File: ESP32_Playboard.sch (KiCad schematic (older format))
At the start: 40 parts, among them J1 USB_B_Micro, J2 TF_PUSH, Q1 Q_NPN_BEC, Q2 Q_NPN_BEC, Q3 Q_NPN_BEC, SW1 SW_SPST, SW2 SW_SPST, U1 AMS1117-3.3, U2 USBLC6-2SC6, U3 CH340G, U4 ESP32-WROVER-I, U5 MPU-6050, U6 SHT30-DIS, Y1 12MHz

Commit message: Finished PCB layout
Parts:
- added H2, H3: MountingHole, MountingHole:MountingHole_3.2mm_M3, symbol Mechanical:MountingHole
- renumbered C8 to C10, C9 to C11, C10 to C8, C11 to C9, U5 to U4, U4 to U5
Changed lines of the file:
@@
 	9800 3900 9800 4150
 $Comp
-L power:GND #PWR011
+L power:GND #PWR010
 U 1 1 62176701
 P 9200 4100
-F 0 "#PWR011" H 9200 3850 50  0001 C CNN
+F 0 "#PWR010" H 9200 3850 50  0001 C CNN
 F 1 "GND" H 9205 3927 50  0000 C CNN
 F 2 "" H 9200 4100 50  0001 C CNN
@@
 $EndComp
 $Comp
-L Sensor_Motion:MPU-6050 U5
+L Sensor_Motion:MPU-6050 U4
 U 1 1 61F460D4
 P 9900 4850
-F 0 "U5" H 9450 5400 50  0000 C CNN
+F 0 "U4" H 9450 5400 50  0000 C CNN
 F 1 "MPU-6050" H 10300 5400 50  0000 C CNN
 F 2 "Sensor_Motion:InvenSense_QFN-24_4x4mm_P0.5mm" H 9900 4050 50  0001 C CNN
@@
 $EndComp
 $Comp
-L Device:C_Small C10
+L Device:C_Small C8
 U 1 1 620A695E
 P 9200 4000
-F 0 "C10" H 9300 4050 50  0000 C CNN
+F 0 "C8" H 9300 4050 50  0000 C CNN
 F 1 "10nF" H 9350 3950 50  0000 C CNN
 F 2 "Capacitor_SMD:C_0603_1608Metric" H 9200 4000 50  0001 C CNN
@@
 Connection ~ 9800 3900
 $Comp
-L Device:C_Small C11
+L Device:C_Small C9
 U 1 1 622611E6
 P 10700 4000
-F 0 "C11" H 10500 4000 50  0000 L CNN
+F 0 "C9" H 10500 4000 50  0000 L CNN
 F 1 "100nF" H 10450 3900 50  0000 L CNN
 F 2 "Capacitor_SMD:C_0603_1608Metric" H 10700 4000 50  0001 C CNN
@@
 Connection ~ 10000 3900
 $Comp
-L power:GND #PWR012
+L power:GND #PWR011
 U 1 1 62270878
 P 10700 4100
-F 0 "#PWR012" H 10700 3850 50  0001 C CNN
+F 0 "#PWR011" H 10700 3850 50  0001 C CNN
 F 1 "GND" H 10705 3927 50  0000 C CNN
 F 2 "" H 10700 4100 50  0001 C CNN
@@
 $EndComp
 $Comp
-L power:GND #PWR021
+L power:GND #PWR020
 U 1 1 62306E82
 P 9900 5550
-F 0 "#PWR021" H 9900 5300 50  0001 C CNN
+F 0 "#PWR020" H 9900 5300 50  0001 C CNN
 F 1 "GND" H 9905 5377 50  0000 C CNN
 F 2 "" H 9900 5550 50  0001 C CNN
@@
 REG_3V3
 $Comp
-L Device:C_Small C8
+L Device:C_Small C10
 U 1 1 61BF902D
 P 2600 4150
-F 0 "C8" H 2800 4100 50  0000 R CNN
+F 0 "C10" H 2800 4100 50  0000 R CNN
 F 1 "22uF" H 2900 4200 50  0000 R CNN
 F 2 "Capacitor_SMD:C_0603_1608Metric" H 2600 4150 50  0001 C CNN
@@
 $EndComp
 $Comp
-L Device:C_Small C9
+L Device:C_Small C11
 U 1 1 61BF9804
 P 2800 4150
-F 0 "C9" H 2700 4100 50  0000 R CNN
+F 0 "C11" H 2700 4100 50  0000 R CNN
 F 1 "100nF" H 2700 4200 50  0000 R CNN
 F 2 "Capacitor_SMD:C_0603_1608Metric" H 2800 4150 50  0001 C CNN
@@
 	2800 4300 2800 4250
 $Comp
-L power:GND #PWR010
+L power:GND #PWR012
 U 1 1 61C2302B
 P 2700 4350
-F 0 "#PWR010" H 2700 4100 50  0001 C CNN
+F 0 "#PWR012" H 2700 4100 50  0001 C CNN
 F 1 "GND" H 2705 4177 50  0000 C CNN
 F 2 "" H 2700 4350 50  0001 C CNN
@@
 IR_RECV
 $Comp
-L power:GND #PWR020
+L power:GND #PWR021
 U 1 1 61CED5C0
 P 4800 5700
-F 0 "#PWR020" H 4800 5450 50  0001 C CNN
+F 0 "#PWR021" H 4800 5450 50  0001 C CNN
 F 1 "GND" H 4805 5527 50  0000 C CNN
 F 2 "" H 4800 5700 50  0001 C CNN
@@
 ESP_RX
 $Comp
-L PlayboardLib:ESP32-WROVER-I U4
+L PlayboardLib:ESP32-WROVER-I U5
 U 1 1 61BE7406
 P 4150 5100
-F 0 "U4" H 4150 6467 50  0000 C CNN
+F 0 "U5" H 4150 6467 50  0000 C CNN
 F 1 "ESP32-WROVER-I" H 4150 6376 50  0000 C CNN
 F 2 "PlayboardLib:XCVR_ESP32-WROVER-I" H 3850 6350 50  0001 L BNN
@@
 	1    0    0    -1
 $EndComp
+$Comp
+L Mechanical:MountingHole H2
+U 1 1 61F4E6C6
+P 11050 600
+F 0 "H2" H 11150 646 50  0000 L CNN
+F 1 "MountingHole" H 11150 555 50  0000 L CNN
+F 2 "MountingHole:MountingHole_3.2mm_M3" H 11050 600 50  0001 C CNN
+F 3 "~" H 11050 600 50  0001 C CNN
+	1    11050 600
+	1    0    0    -1
+$EndComp
+$Comp
+L Mechanical:MountingHole H3
+U 1 1 61F5140B
+P 10800 600
+F 0 "H3" H 10900 646 50  0000 L CNN
+F 1 "MountingHole" H 10900 555 50  0000 L CNN
+F 2 "MountingHole:MountingHole_3.2mm_M3" H 10800 600 50  0001 C CNN
+F 3 "~" H 10800 600 50  0001 C CNN
+	1    10800 600
+	1    0    0    -1
+$EndComp

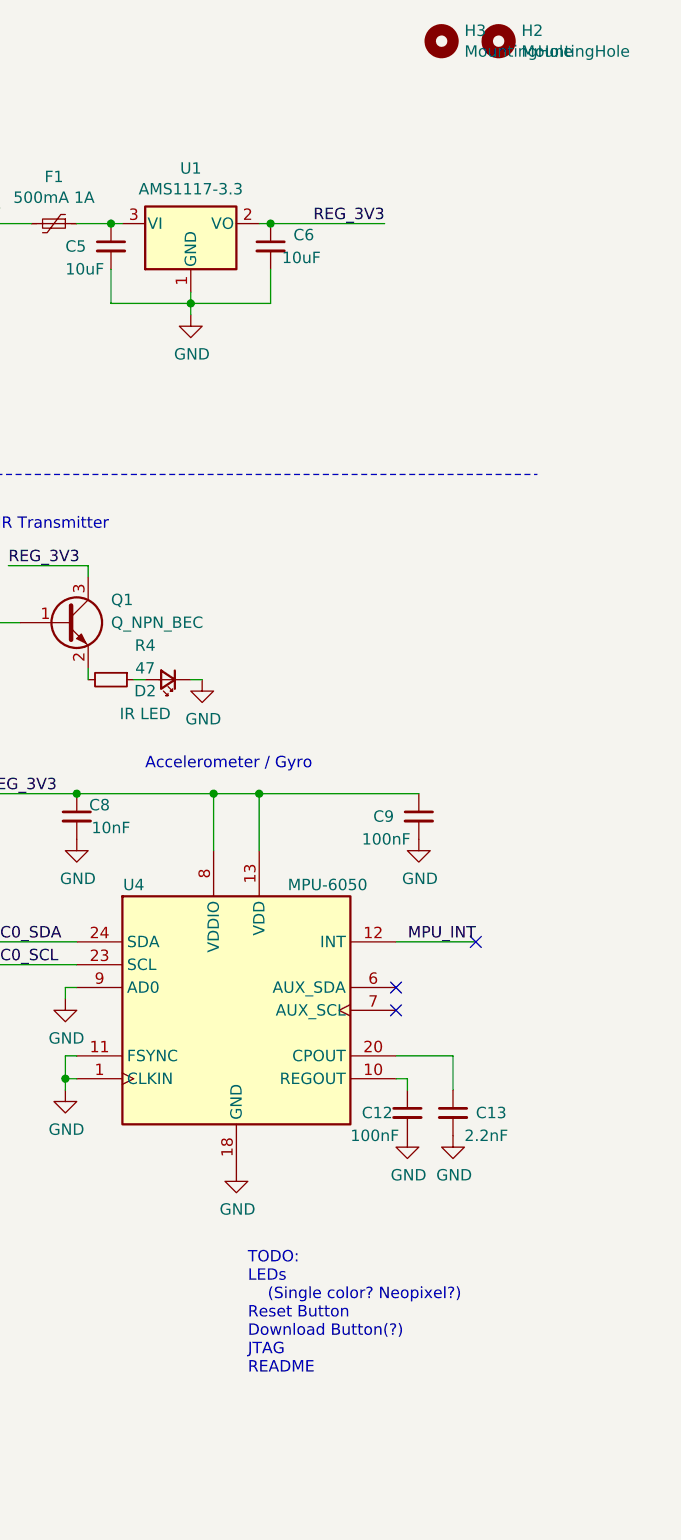
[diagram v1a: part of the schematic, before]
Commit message: Exported Gerber and started Readme
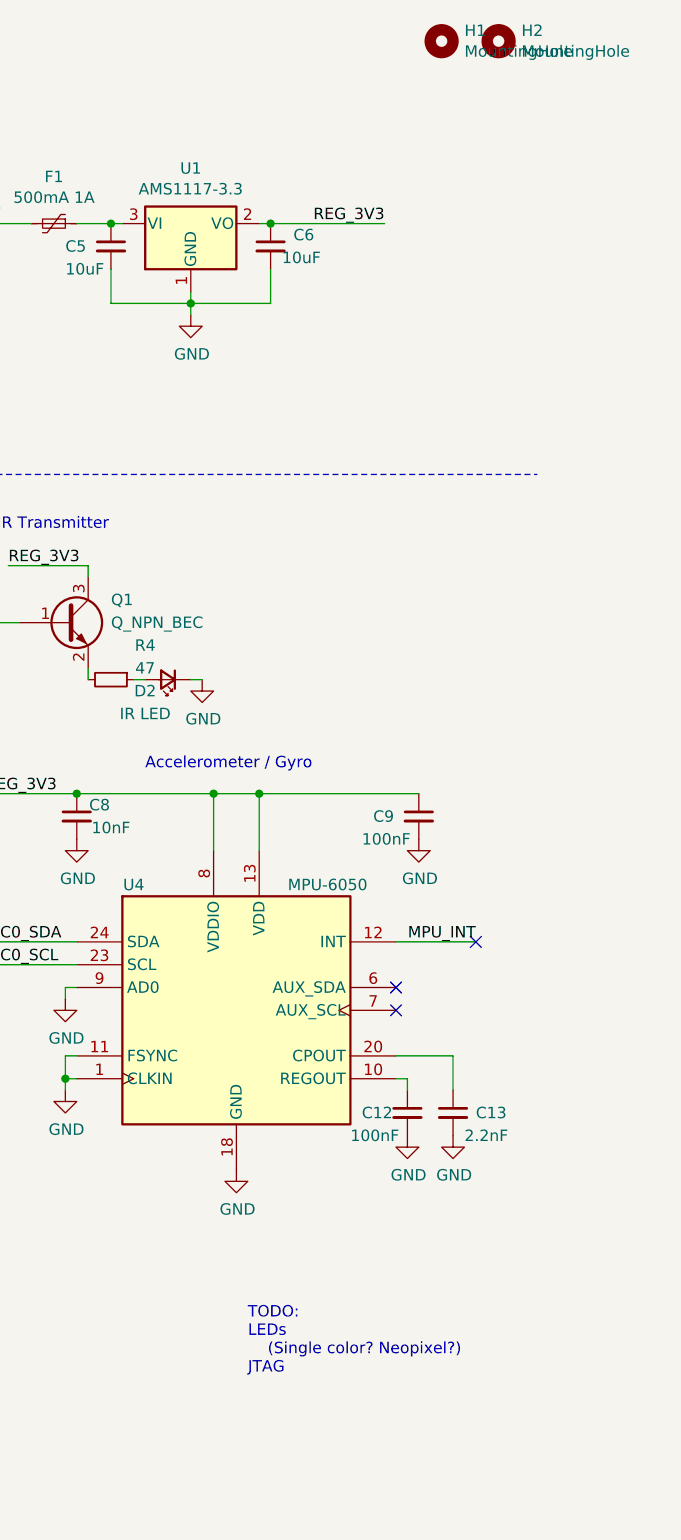
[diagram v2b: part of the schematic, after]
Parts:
- renumbered H3 to H1
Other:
- note added: "TODO:\nLEDs\n (Single color? Neopixel?)\nJTAG"
- note removed: "TODO:\nLEDs\n (Single color? Neopixel?)\nReset Button\nDownload Button(?)\nJTAG\nREADME"
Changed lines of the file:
@@
 $EndDescr
 Text Notes 9950 6450 0    50   ~ 0
-TODO:\nLEDs\n    (Single color? Neopixel?)\nReset Button\nDownload Button(?)\nJTAG\nREADME
+TODO:\nLEDs\n    (Single color? Neopixel?)\nJTAG
 $Comp
 L Regulator_Linear:AMS1117-3.3 U1
@@
 $EndComp
 $Comp
-L Mechanical:MountingHole H3
+L Mechanical:MountingHole H1
 U 1 1 61F5140B
 P 10800 600
-F 0 "H3" H 10900 646 50  0000 L CNN
+F 0 "H1" H 10900 646 50  0000 L CNN
 F 1 "MountingHole" H 10900 555 50  0000 L CNN
 F 2 "MountingHole:MountingHole_3.2mm_M3" H 10800 600 50  0001 C CNN

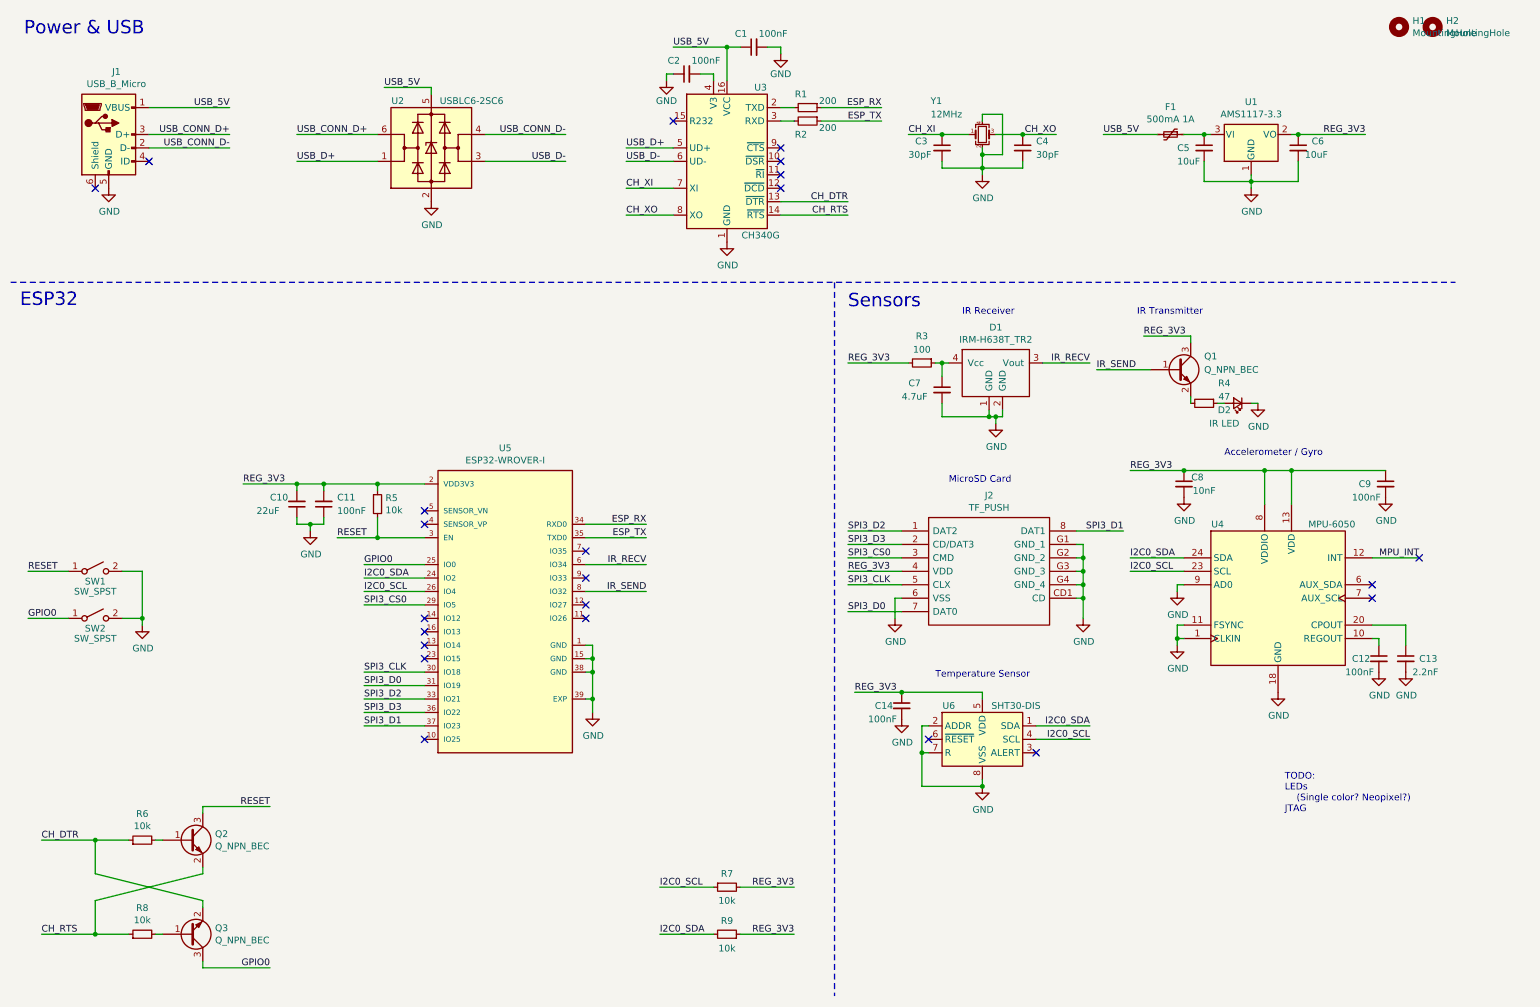
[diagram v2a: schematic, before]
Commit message: Rearranged the schematic
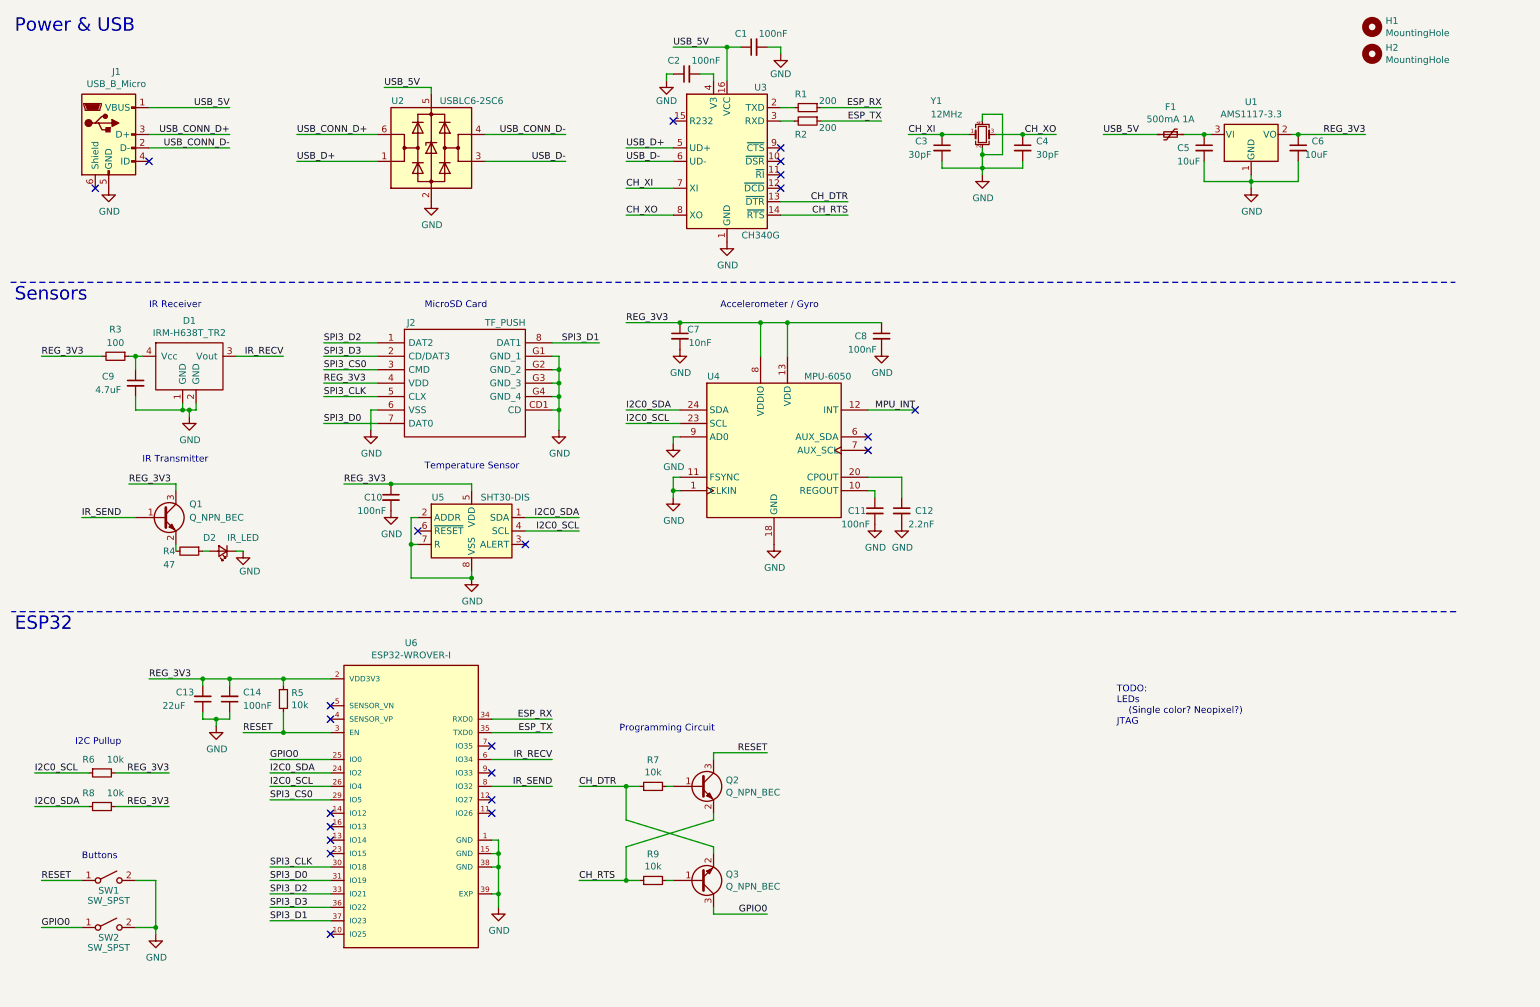
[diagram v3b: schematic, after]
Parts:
- D2: value IR LED -> IR_LED
- renumbered C14 to C10, C12 to C11, C13 to C12, C10 to C13, C11 to C14, C8 to C7, C9 to C8, C7 to C9, R7 to R6, R6 to R7, R9 to R8, R8 to R9, U6 to U5, U5 to U6
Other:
- note added: "Buttons"
- note added: "I2C Pullup"
- note added: "Programming Circuit"
- moved on the sheet: C10, C11, C12, C13, C14, C7, C8, C9, D1, D2, H1, H2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

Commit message: Added magnetometer, attached interrupts, added silkscreen orientation
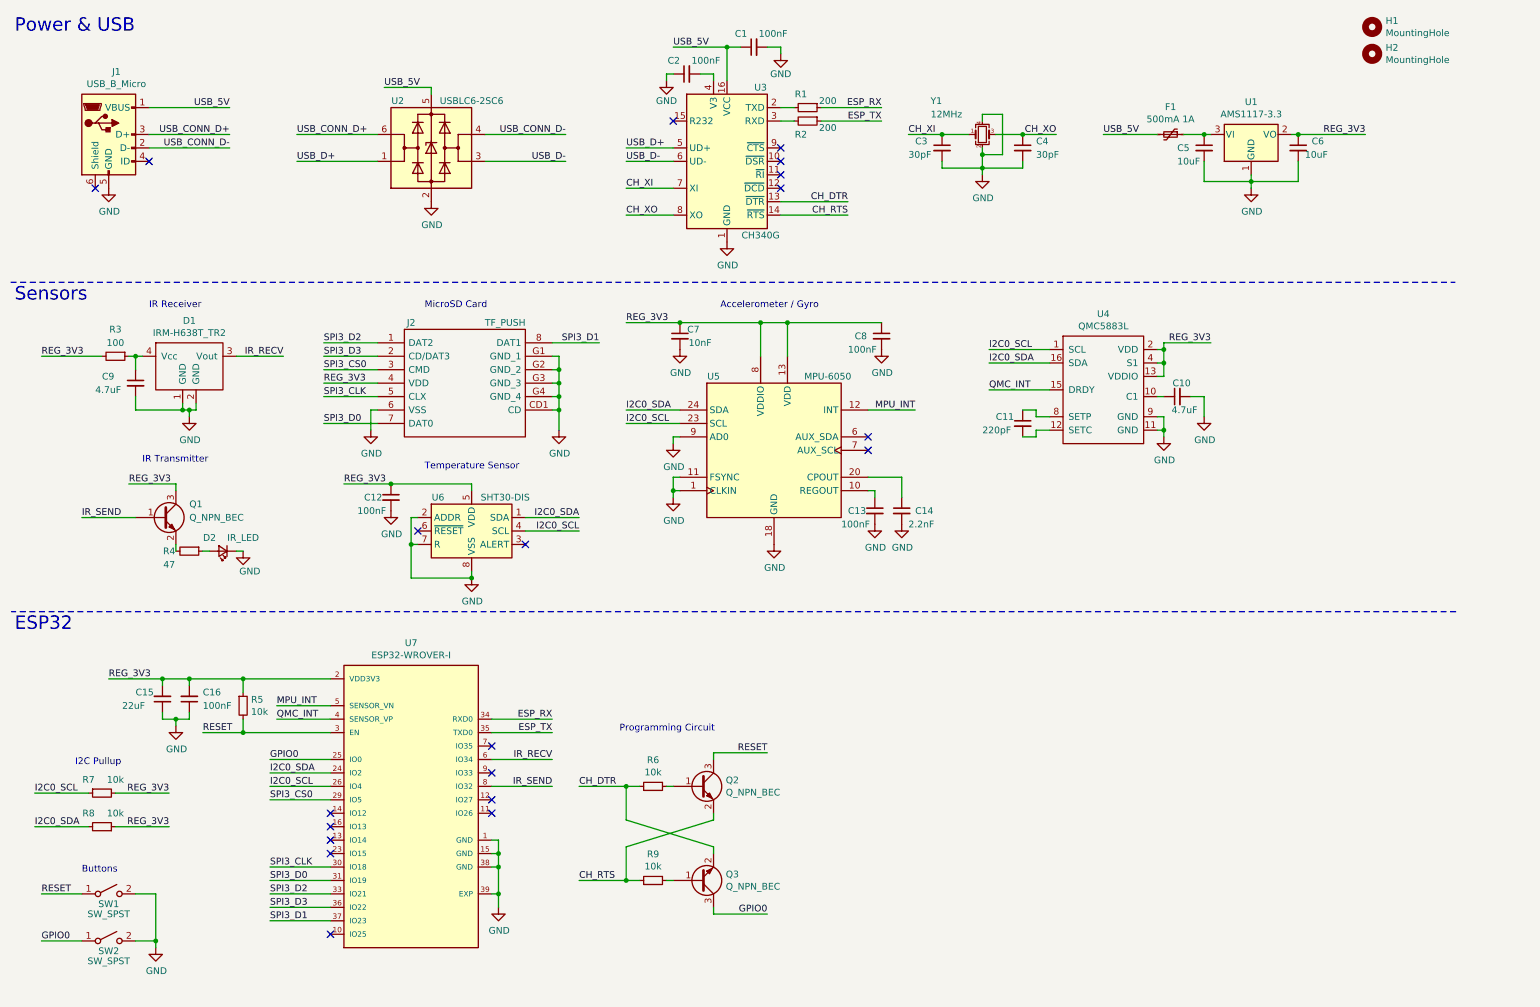
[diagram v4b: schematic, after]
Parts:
- added C10: 4.7uF, Capacitor_SMD:C_0603_1608Metric, symbol Device:C_Small
- added C11: 220pF, Capacitor_SMD:C_0603_1608Metric, symbol Device:C_Small
- added U4: QMC5883L, Package_LGA:LGA-16_3x3mm_P0.5mm, symbol PlayboardLib:QMC5883L
- renumbered C10 to C12, C11 to C13, C12 to C14, C13 to C15, C14 to C16, R7 to R6, R6 to R7, U4 to U5, U5 to U6, U6 to U7
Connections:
- net GND: now also C10.2, U4.11 (GND), U4.9 (GND)
- net I2C0_SCL: now also U4.1 (SCL)
- net I2C0_SDA: now also U4.16 (SDA)
- net MPU_INT: now also U7.5 (SENSOR_VN)
- net REG_3V3: now also U4.13 (VDDIO), U4.2 (VDD), U4.4 (S1)
- net QMC_INT: now reaches U7.4 (SENSOR_VP)
- net QMC_INT: now also U4.15 (DRDY)
- new net: C10.1, U4.10 (C1)
- new net: C11.2, U4.12 (SETC)
- new net: C11.1, U4.8 (SETP)
- no-connect marks 23 -> 20
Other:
- note removed: "TODO:\nLEDs\n (Single color? Neopixel?)\nJTAG"
- moved on the sheet: C15, C16, R5, R7, R8, SW1, SW2
